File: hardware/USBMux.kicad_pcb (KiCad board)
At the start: 4 copper layers, 80 x 40 mm, 37 parts, among them J1 USB_0, J2 USB_1, J3 USB_A, J4 USB_C_Receptacle, SW1 SW_Push, SW2 SW_Push, U1 STM32F042F4Px, U10 USBLC6-2SC6, U2 FSUSB42MUX, U3 TPS2051CDBV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

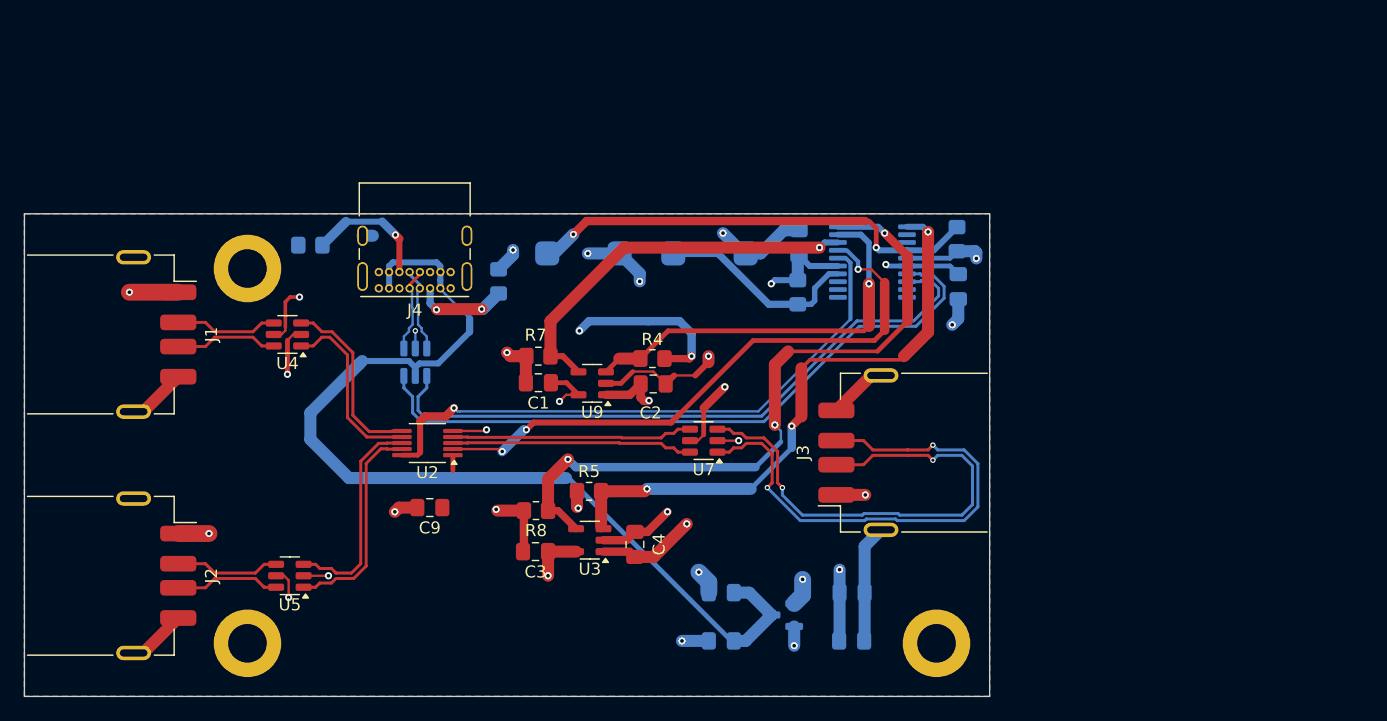
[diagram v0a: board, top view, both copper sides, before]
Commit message: Update PCB, fix bug in BOOT0
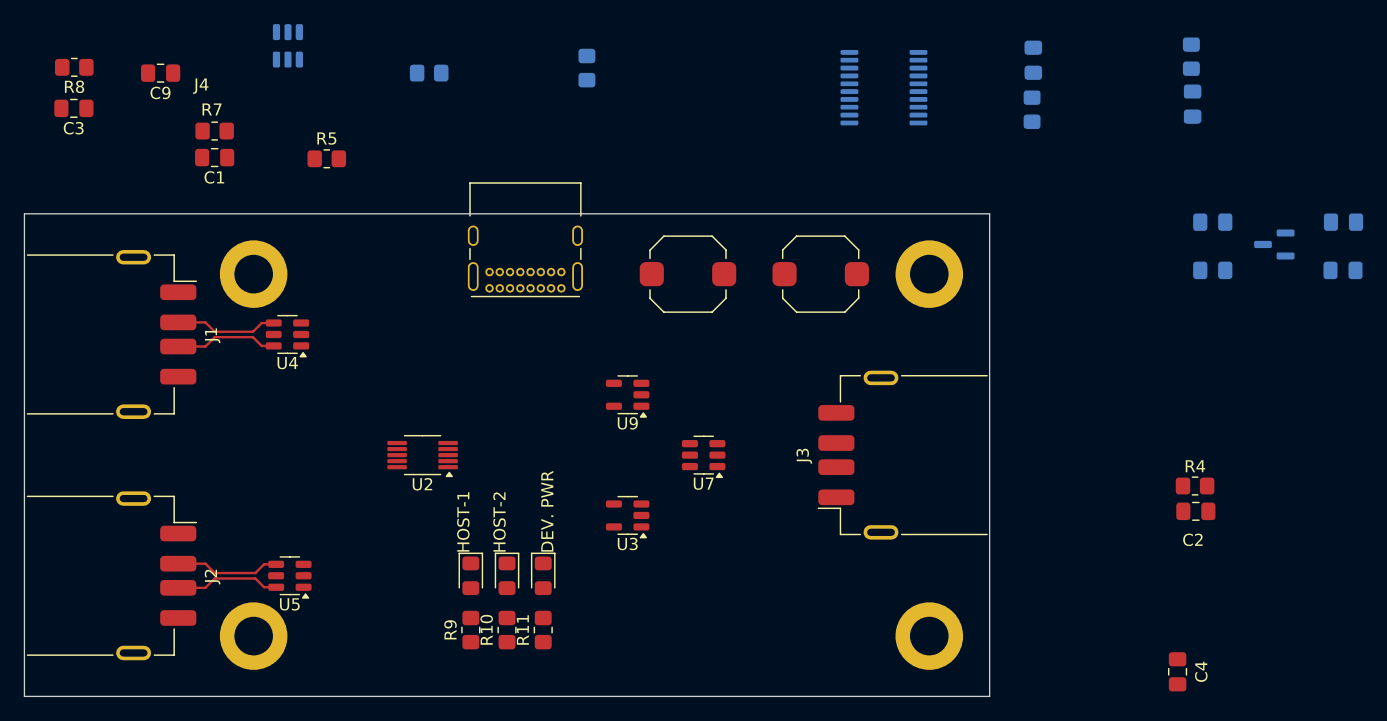
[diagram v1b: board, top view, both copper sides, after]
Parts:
- added D1: LED, LED_SMD:LED_0805_2012Metric_Pad1.15x1.40mm_HandSolder, F.Cu at (99.0, 92.2)
- added D2: LED, LED_SMD:LED_0805_2012Metric_Pad1.15x1.40mm_HandSolder, F.Cu at (102.0, 92.2)
- added D3: LED, LED_SMD:LED_0805_2012Metric_Pad1.15x1.40mm_HandSolder, F.Cu at (105.0, 92.2)
- added H4: MountingHole_Pad, MountingHole:MountingHole_3.2mm_M3_DIN965_Pad, F.Cu at (137.0, 67.2)
- added R10: 150, Resistor_SMD:R_0805_2012Metric_Pad1.20x1.40mm_HandSolder, F.Cu at (102.0, 96.7)
- added R11: 150, Resistor_SMD:R_0805_2012Metric_Pad1.20x1.40mm_HandSolder, F.Cu at (105.0, 96.7)
- added R9: 150, Resistor_SMD:R_0805_2012Metric_Pad1.20x1.40mm_HandSolder, F.Cu at (99.0, 96.7)
- SW1, SW2: moved to F.Cu
- moved R8 53.0 mm to (66.1, 50.0)
- moved C3 53.0 mm to (66.1, 53.4)
- moved C7 51.0 mm to (171.3, 62.9)
- moved C8 51.0 mm to (171.3, 66.9)
- moved C6 51.0 mm to (160.5, 66.9)
- moved C5 51.0 mm to (160.5, 62.9)
- moved U8 51.0 mm to (165.6, 64.7)
- moved C4 46.2 mm to (157.6, 100.1)
- moved C2 46.2 mm to (159.1, 86.8)
- moved R4 46.2 mm to (159.0, 84.7)
- moved C9 42.4 mm to (73.3, 50.5)
- moved R5 35.1 mm to (87.0, 57.6)
- moved C1 32.7 mm to (77.7, 57.5)
- moved R7 32.7 mm to (77.7, 55.3)
- moved U10 28.3 mm to (83.8, 48.3)
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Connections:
- U1 pad 1: unconnected-(U1-PB8-Pad1) -> /BOOT0
- U1 pad 12: unconnected-(U1-PA6-Pad12) -> /HOST_1_ACTIVE
- U1 pad 13: unconnected-(U1-PA7-Pad13) -> /HOST_2_ACTIVE
- U1 pad 14: /BOOT0 -> unconnected-(U1-PB1-Pad14)
- U1 pad 19: unconnected-(U1-PA13-Pad19) -> /DEVICE_POWERED
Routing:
- net GNDREF: track 97.4 -> 0.00 mm, vias 17 -> 0
- net VBUS: track 82.1 -> 0.00 mm
- net /EN_1: track 58.0 -> 0.00 mm, vias 3 -> 0
- net /USB_CTRL_DATA_N: track 56.4 -> 0.00 mm
- net /USB_CTRL_DATA_P: track 54.2 -> 0.00 mm
- net /MUX_nOE: track 49.5 -> 0.00 mm, vias 1 -> 0
- net /MUX_SEL: track 49.4 -> 0.00 mm, vias 3 -> 0
- net /nFLT_1: track 49.4 -> 0.00 mm, vias 3 -> 0
- net /USB_D_P: track 43.8 -> 0.00 mm, vias 2 -> 0
- net /USB_D_N: track 41.9 -> 0.00 mm, vias 2 -> 0
- net /BOOT0: track 38.4 -> 0.00 mm, vias 2 -> 0
- net /nFLT_0: track 33.1 -> 0.00 mm, vias 1 -> 0
- net /EN_0: track 32.3 -> 0.00 mm, vias 1 -> 0
- net VCC: track 30.1 -> 0.00 mm, vias 6 -> 0
- net VBUS_USB_0: track 27.7 -> 0.00 mm, vias 5 -> 0
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- removed copper zone on B.Cu, net GNDREF
- removed copper zone on In1.Cu, net GNDREF
- removed copper zone on In2.Cu, net VBUS_DEV
- removed copper zone on In2.Cu, net VBUS_USB_0
- removed copper zone on In2.Cu, net VBUS_USB_1
- removed copper zone on F.Cu, net VCC
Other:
- board text added: "DEV. PWR"
- board text added: "HOST-1"
- board text added: "HOST-2"
